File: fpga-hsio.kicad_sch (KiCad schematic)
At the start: 3 parts, among them U1 MPFS250T-FCVG484, Y5 Oscillator_50MHz_ECS_1612MV

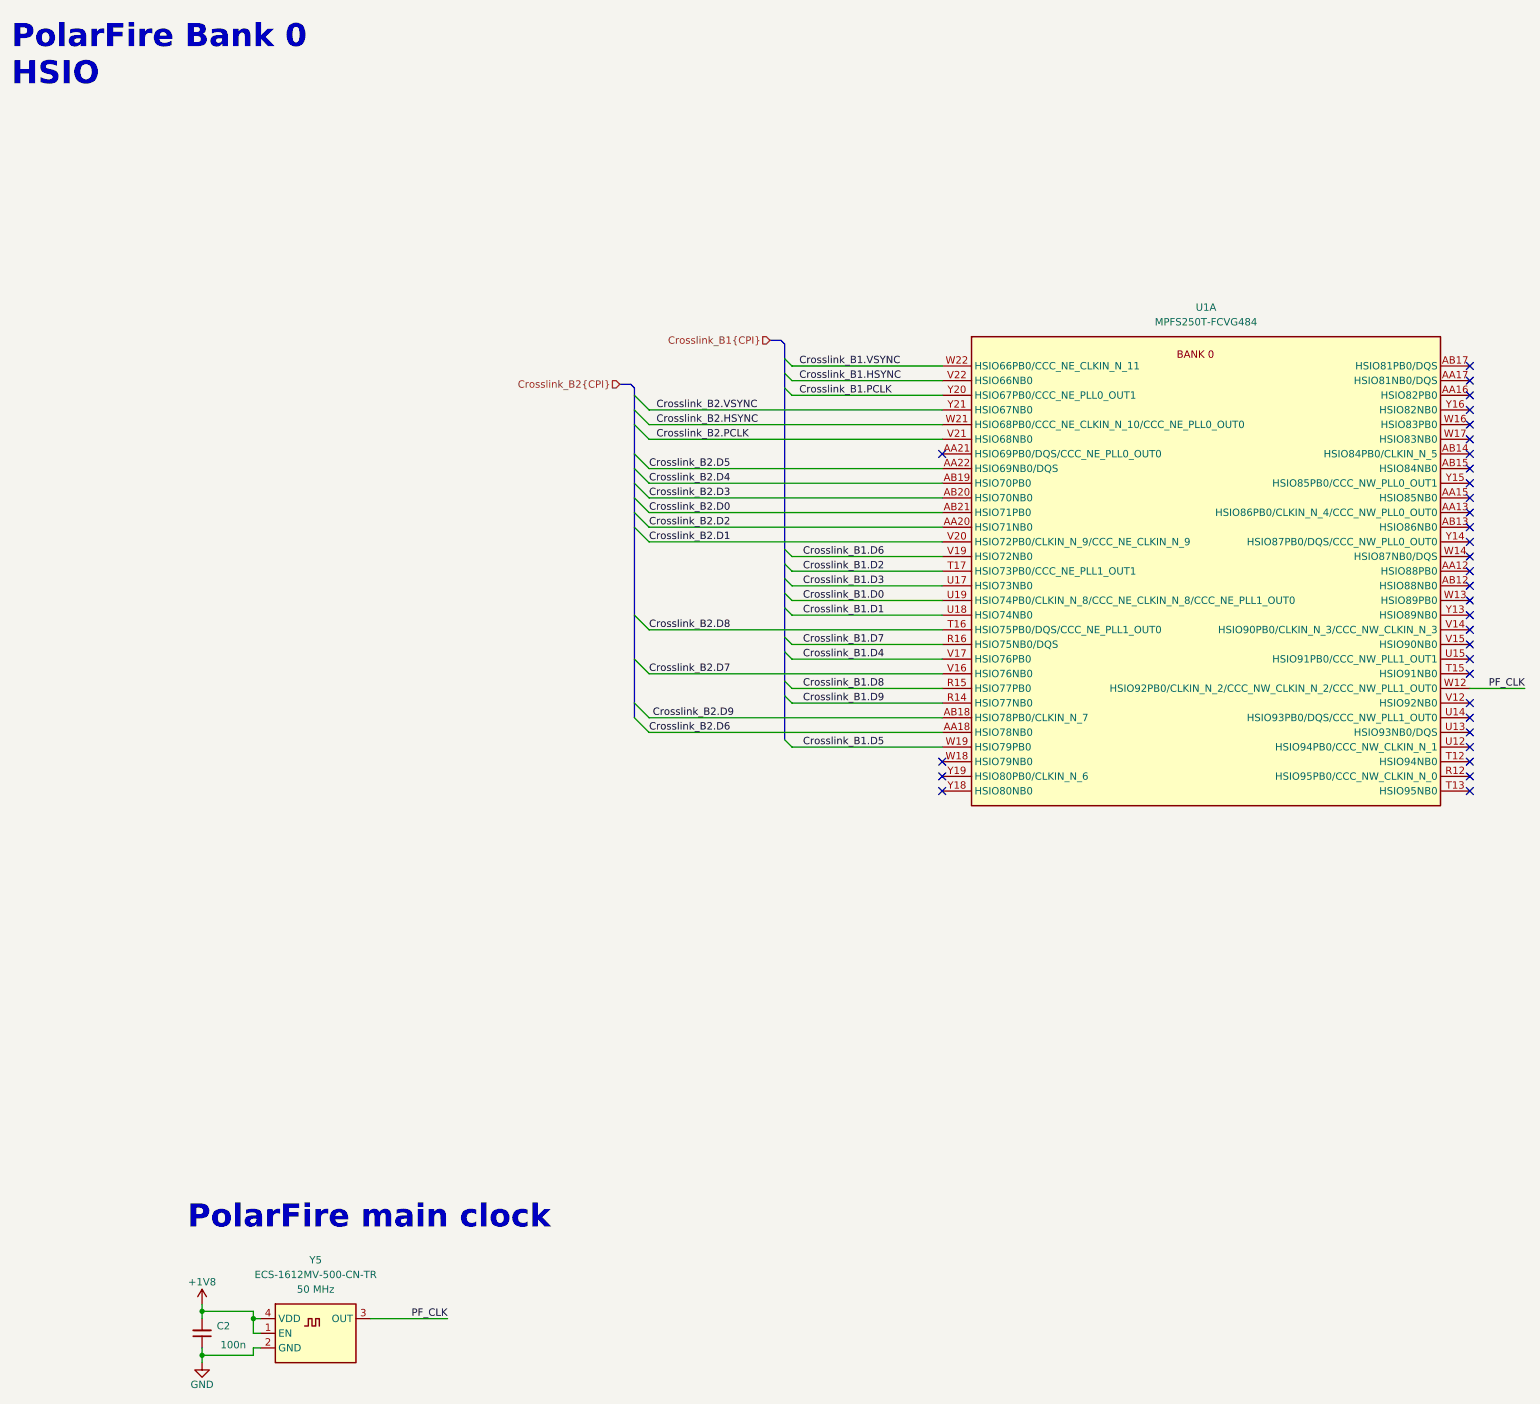
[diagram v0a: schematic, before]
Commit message: [#59910] Align buses, updated symbols and clean ERC
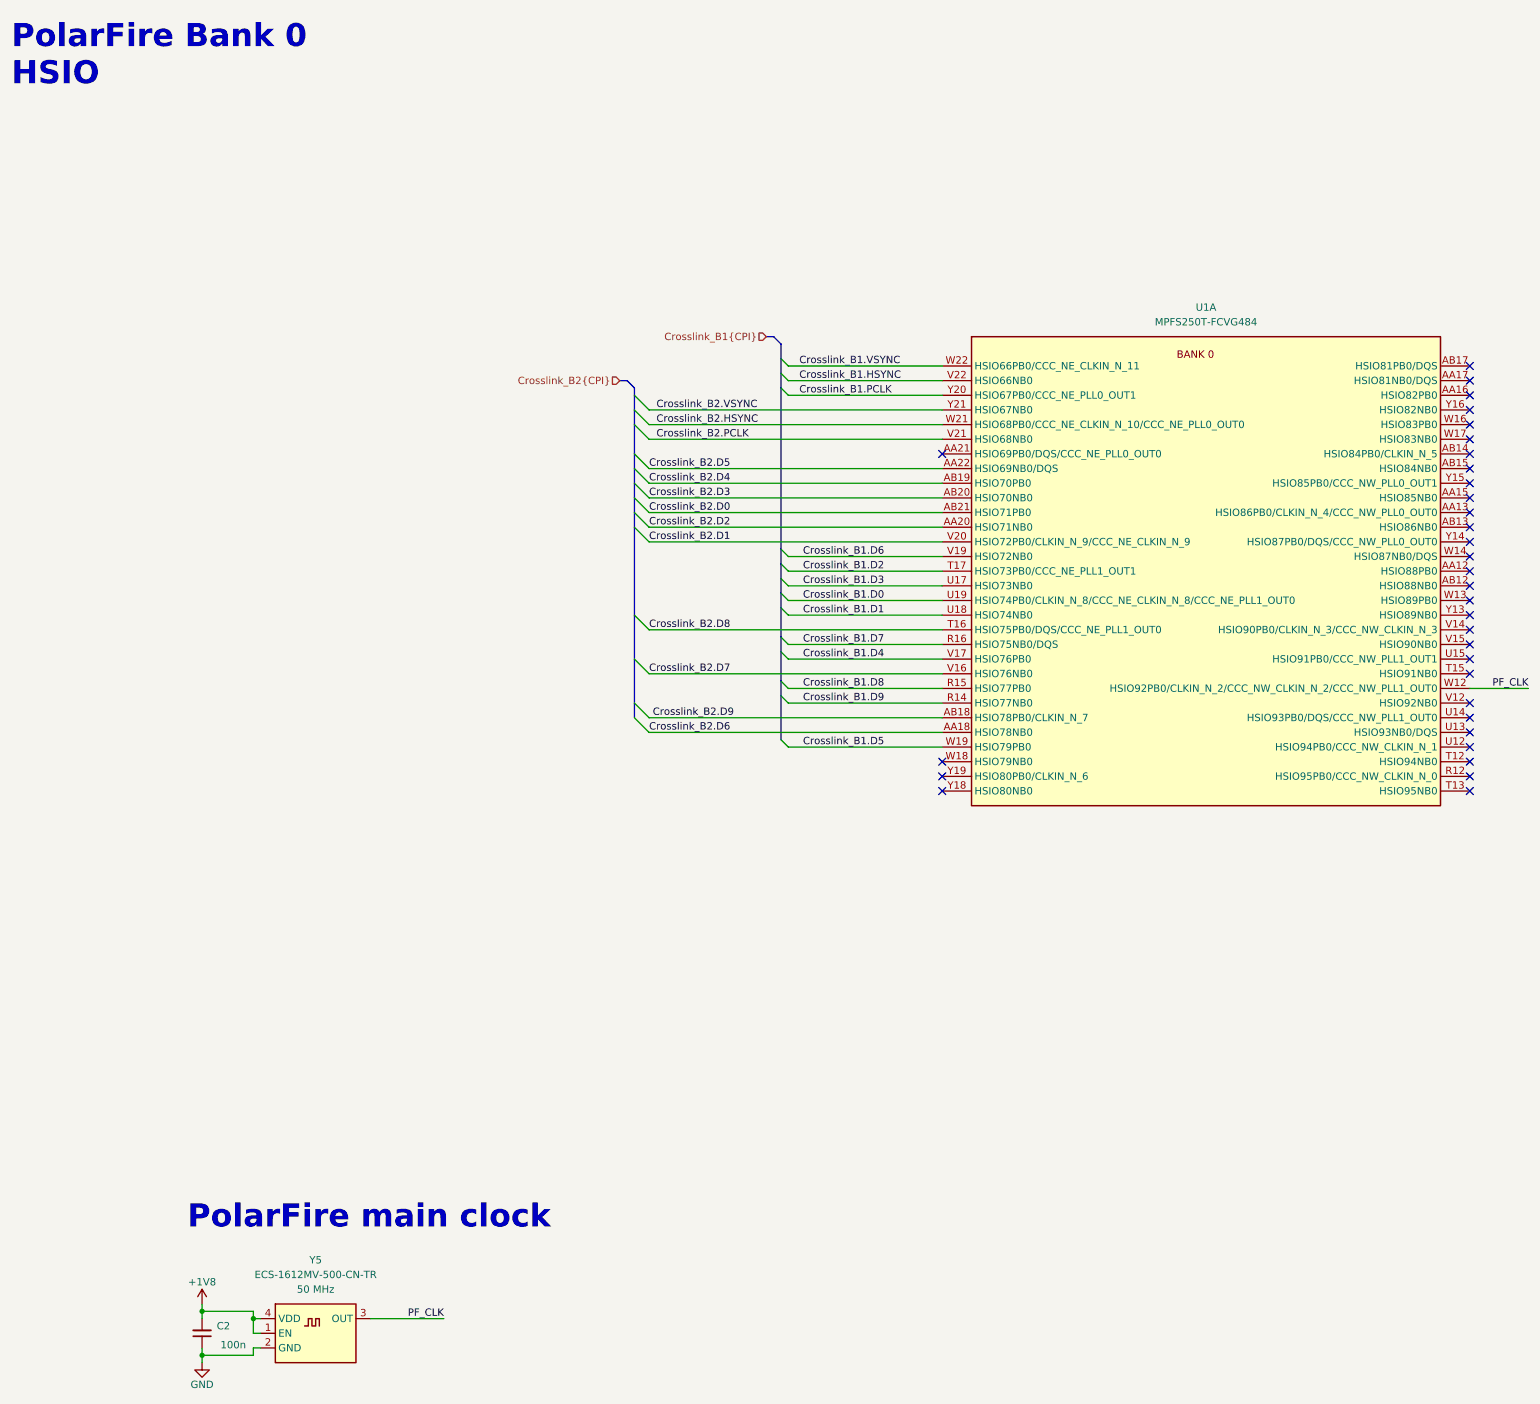
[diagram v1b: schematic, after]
